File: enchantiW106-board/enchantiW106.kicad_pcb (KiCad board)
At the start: 4 copper layers, 62.2 x 25.4 mm, 65 parts, among them J1 USB_C_Receptacle_USB2.0, SW1 B3U-1000P, SW2 B3U-1000P, U1 USBLC6-2P6, U11 MAX17262REWL+T, U12 BQ25185DLHR, U13 ICM-42670-P, U2 MMC5633NJL, U3 IRIS-W106-00B, U4 NCP167AMX330TBG, U5 CP2102N-Axx-xQFN20, U6 ESP-PSRAM64, U9 NCP167AMX330TBG

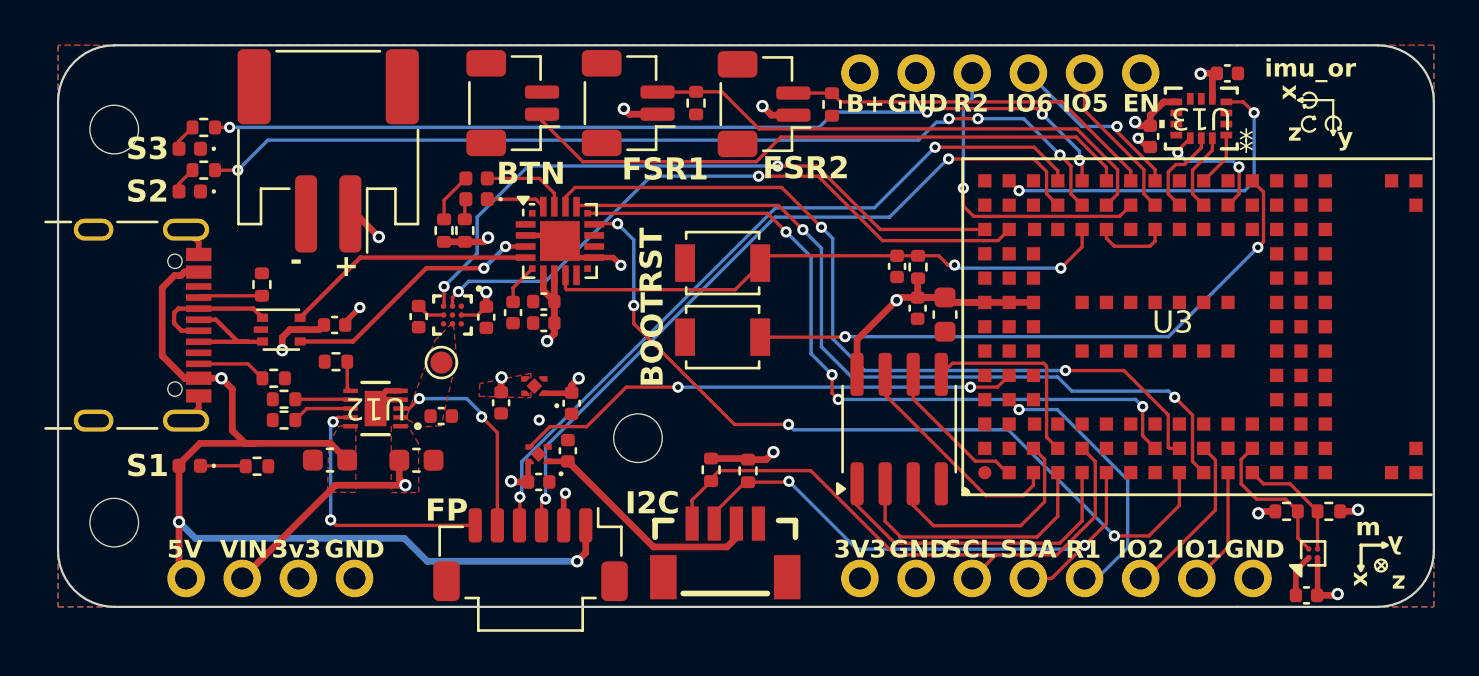
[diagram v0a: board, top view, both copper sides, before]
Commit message: Fixed mistakes with revision 1 of the board, removed traces from inner layers
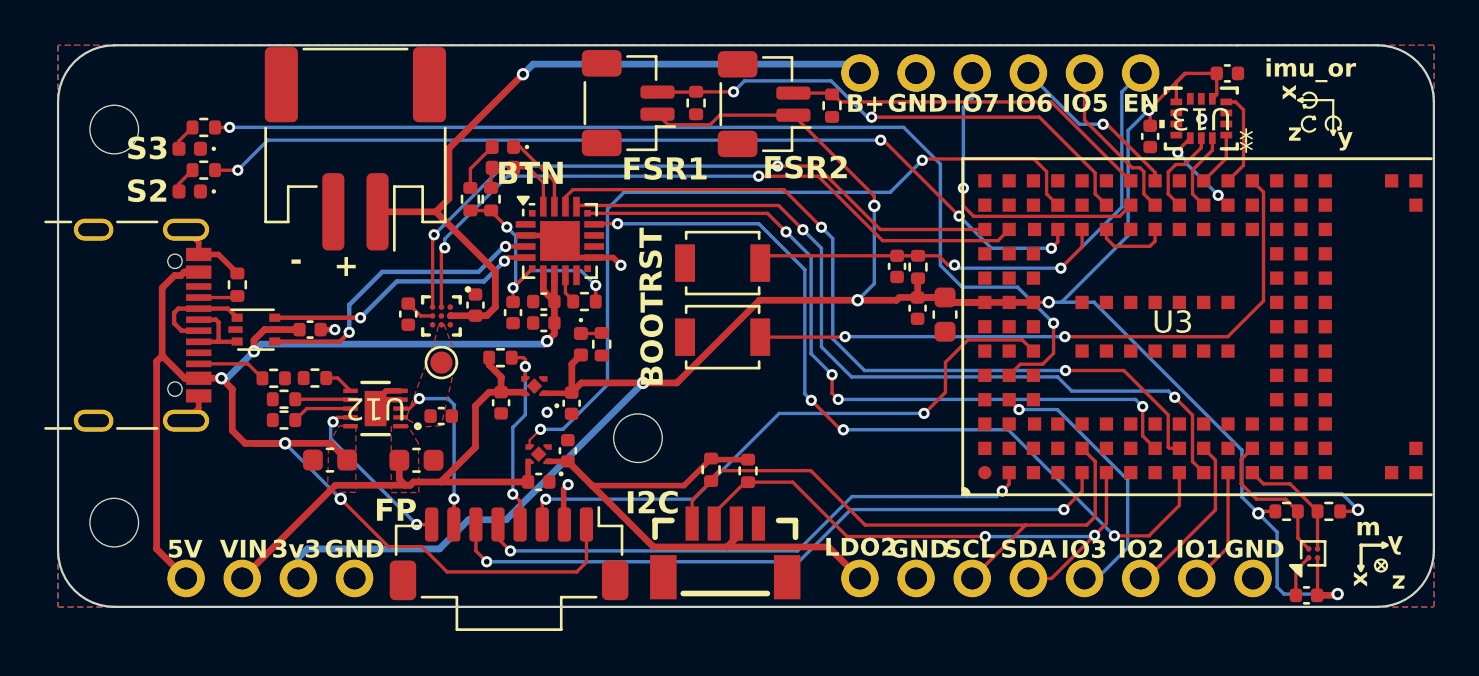
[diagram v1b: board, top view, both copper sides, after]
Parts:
- removed ANG2: CONN HEADER SMD 2POS 1MM, ENCHANTI_connectors:Molex_Pico-Clasp_2pin_Vertical
- removed FP1: CONN HEADER SMD 6POS 1MM, ENCHANTI_connectors:Molex_Pico-Clasp_501331-0607_1x06-1MP_P1.00mm_Vertical
- removed U6: ESP-PSRAM64, Package_SO:SOIC-8_3.9x4.9mm_P1.27mm
- added FP2: CONN HEADER SMD 6POS 1MM, Connector_Molex:Molex_Pico-Clasp_501331-0807_1x08-1MP_P1.00mm_Vertical, F.Cu at (113.1, 71.3)
- added R17: 10k, Resistor_SMD:R_0402_1005Metric, F.Cu at (112.7, 62.4)
- added R18: 1k, Resistor_SMD:R_0402_1005Metric, F.Cu at (116.5, 59.9)
- R1, R2: value 10k -> 1k
- R15: value 0.3k -> 0.43k
- moved CHARGLED1 18.5 mm to (116.4, 61.8), turned to -90 degrees
- moved R3 16.5 mm to (117.3, 61.8), turned to -90 degrees
- moved R14 1.85 mm to (111.4, 55.2)
- moved R16 1.85 mm to (112.3, 55.2)
- moved STATLED3 1.85 mm to (112.8, 53.8)
- moved STATLED4 1.85 mm to (112.8, 52.9)
- moved BT1 1.23 mm to (106.2, 52.9)
- moved R21 1.20 mm to (104.3, 63.3)
- moved U1 1.15 mm to (101.7, 61.1)
- moved C15 1.13 mm to (104.1, 61.1)
- moved R7 1.11 mm to (100.8, 59.1)
- moved C7 0.74 mm to (111.6, 60.0), turned to 90 degrees
- moved U11 0.50 mm to (110.0, 60.5)
- moved C8 0.48 mm to (108.5, 60.4)
- moved R2 0.06 mm to (127.7, 51.0), turned to 90 degrees
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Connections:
- net /BTN_FP renamed /IO29
- BOARDLAYOUT1 pad 2.1: +3V3 -> 3V3_AUX
- C1 pad 1: Net-(U5-VDD) -> VDD
- CHARGLED1 pad 2: VUSB -> +3V3
- R1 pad 1: /FSR1 -> GND
- R1 pad 2: GND -> /FSR1
- R12 pad 2: +3V3 -> 3V3_AUX
- R13 pad 2: +3V3 -> 3V3_AUX
- R14 pad 2: +3V3 -> VDD
- R16 pad 2: +3V3 -> VDD
- R2 pad 1: /FSR2 -> GND
- R2 pad 2: GND -> /FSR2
- U3 pad A2: /RCLK -> /LED1
- U3 pad A3: /RD3 -> unconnected-(U3A-QSPI_RD3-PadA3)
- U3 pad A4: /RD1 -> unconnected-(U3A-QSPI_RD1-PadA4)
- U3 pad A5: /RCE -> /LED2
- U3 pad B3: /RD2 -> unconnected-(U3A-QSPI_RD2-PadB3)
- U3 pad B4: /RD0 -> unconnected-(U3A-QSPI_RD0-PadB4)
- U3 pad E2: /LDO_EN -> /ORANGELED
- U3 pad F3: unconnected-(U3A-RMII_CLK-PadF3) -> /BTN
- U3 pad K3: /LED3 -> unconnected-(U3A-GPIO[61]-PadK3)
- U3 pad L4: unconnected-(U3A-RMII_INT-PadL4) -> /BLUELED
- U3 pad M3: /LED4 -> unconnected-(U3A-GPIO[52]-PadM3)
- U3 pad M4: /LED1 -> /LDO_EN
- U3 pad M5: /BLUELED -> unconnected-(U3A-GPIO[48]-PadM5)
- U3 pad N11: unconnected-(U3A-GPIO[1]-PadN11) -> /IMU_INT
- U3 pad N2: /IMU_INT -> unconnected-(U3A-GPIO[54]-PadN2)
- U3 pad N4: /LED2 -> unconnected-(U3A-GPIO[51]-PadN4)
- U3 pad N5: /ORANGELED -> unconnected-(U3A-GPIO[49]-PadN5)
- U3 pad N6: /BTN -> unconnected-(U3A-GPIO[47]-PadN6)
- U4 pad 3: SYS -> /MAIN_LDO_EN
- U5 pad 6: Net-(U5-VDD) -> VDD
- U5 pad 9: /EN -> /RST
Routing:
- net +3V3: track 38.3 -> 115.5 mm, vias 11 -> 8
- net /RCE: track 14.5 -> 0.00 mm
- net 3V3_AUX: track 11.0 -> 25.1 mm
- net /LDO_EN: track 23.0 -> 35.6 mm
- net SYS: track 12.7 -> 25.2 mm, vias 3 -> 0
- net /RD1: track 12.2 -> 0.00 mm
- net VDD: track 0.00 -> 11.9 mm, vias 0 -> 3
- net /IMU_INT: track 16.0 -> 4.43 mm, vias 2 -> 0
- net /EN: track 37.6 -> 26.5 mm
- net /RD2: track 10.4 -> 0.00 mm
- net /RD3: track 10.3 -> 0.00 mm
- net /MAIN_LDO_EN: track 0.00 -> 9.04 mm, vias 0 -> 2
- net /RD0: track 8.95 -> 0.00 mm
- net +BATT: track 25.0 -> 33.7 mm, vias 2 -> 1
- net /LED1: track 33.7 -> 25.8 mm
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- added copper zone on In2.Cu, net GND
- removed copper zone on In2.Cu, net +3V3
- removed copper zone on In2.Cu, net +BATT
- removed copper zone on In2.Cu, net SYS
- removed copper zone on In2.Cu, net VUSB
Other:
- board text added: "IO3"
- board text added: "IO7"
- board text added: "LDO2"
- board text removed: "3V3"
- board text removed: "BTN IO9"
- board text removed: "R1"
- board text removed: "R2"
- board text removed: "S1"

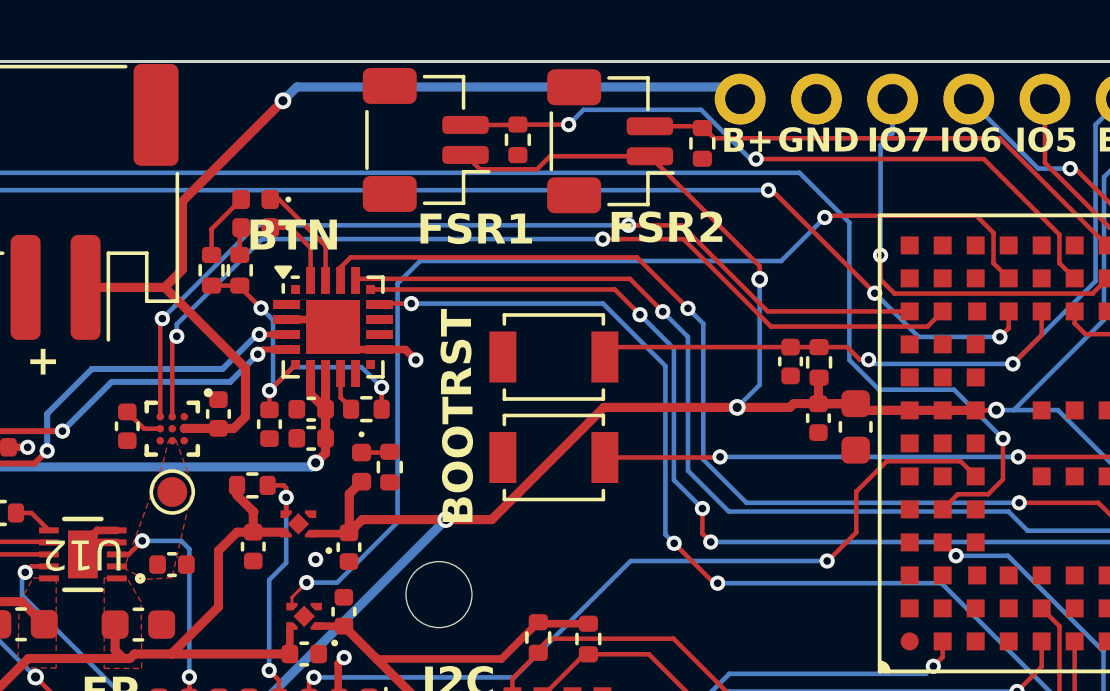
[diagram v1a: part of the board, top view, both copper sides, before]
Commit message: change board designto 2 layer board, fix wrong connection for fuel gauge
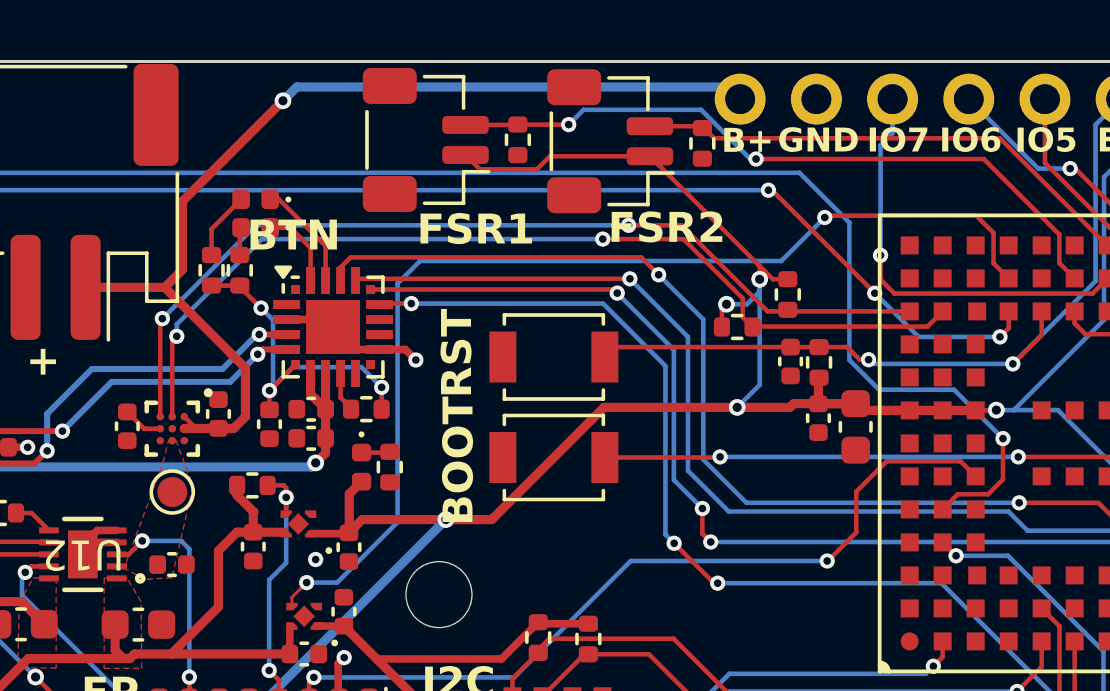
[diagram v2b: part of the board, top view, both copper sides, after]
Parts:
- added R19: 2k2, Resistor_SMD:R_0402_1005Metric, F.Cu at (128.9, 57.1)
- added R20: 2k2, Resistor_SMD:R_0402_1005Metric, F.Cu at (130.6, 56.0)
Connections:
- U11 pad A1: GND -> +BATT
- U11 pad B2: unconnected-(U11-ALRT-PadB2) -> GND
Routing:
- net +3V3: track 115.5 -> 119.3 mm, vias 8 -> 9
- net +BATT: track 33.7 -> 34.4 mm
- removed copper zone on In1.Cu, net GND
- removed copper zone on In2.Cu, net GND
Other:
- copper layers 4 -> 2

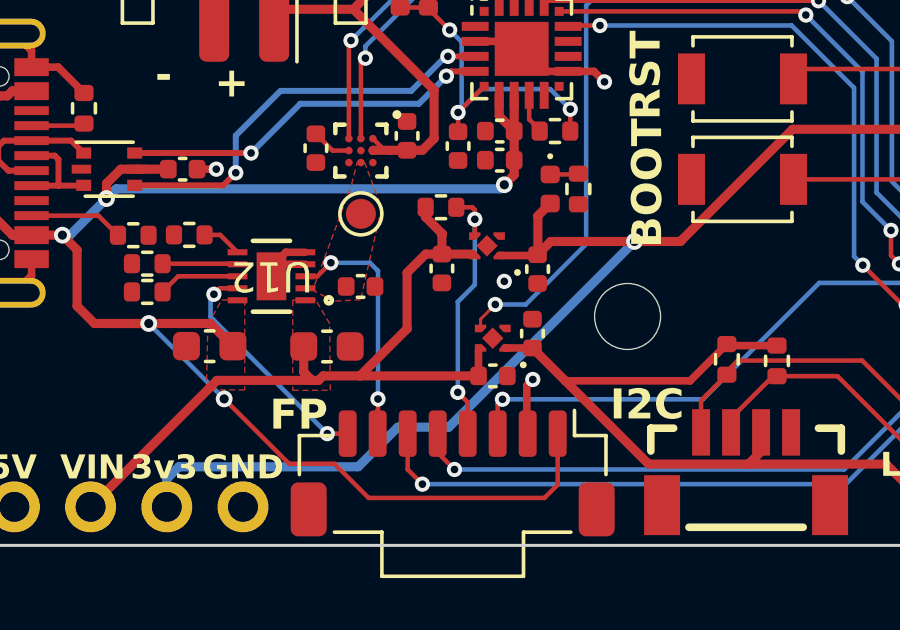
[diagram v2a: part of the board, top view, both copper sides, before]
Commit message: updated manufacturing files for enchantiW106, removed unused board files
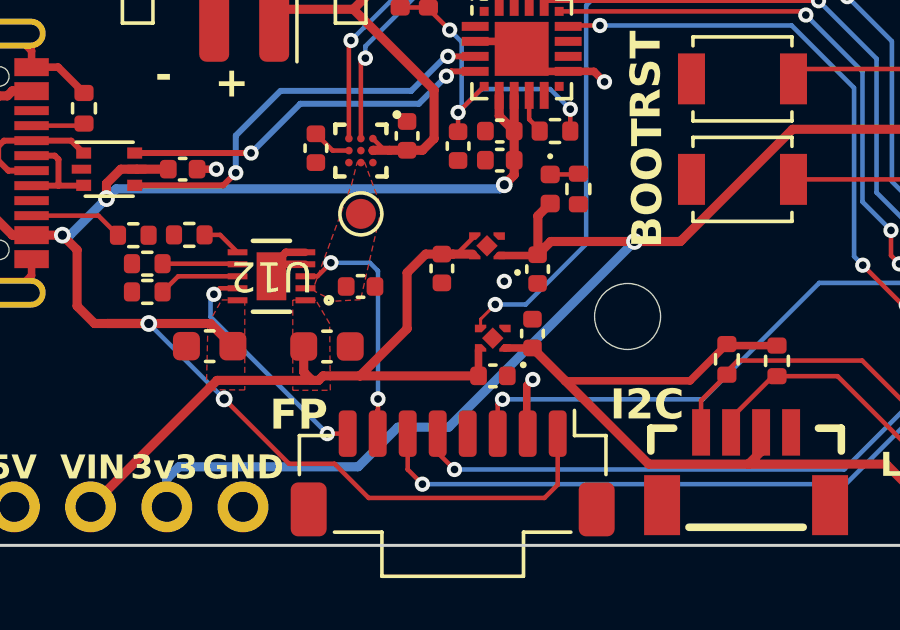
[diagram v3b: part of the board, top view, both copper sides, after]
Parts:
- removed R17: 10k, Resistor_SMD:R_0402_1005Metric
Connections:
- FP2 pad 4: /MAIN_LDO_EN -> unconnected-(FP2-Pin_4-Pad4)
- U4 pad 3: /MAIN_LDO_EN -> SYS
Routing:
- net /MAIN_LDO_EN: track 9.04 -> 0.00 mm, vias 2 -> 0
- net SYS: track 25.2 -> 24.4 mm
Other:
- board text removed: "T-Stick Axis"
- board text removed: "X"
- board text removed: "Y"
